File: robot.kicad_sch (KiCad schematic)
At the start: 31 parts, among them M1 MOTOR, M2 MOTOR, M3 MOTOR, M4 MOTOR, M5 MOTOR, M6 SERVO, U1 BUCKCONVERTER, U12 MEEN3230_POWER_BOARD, U2 TCS3200, U3 XBEE_DONGLE, U6 SHARPDISTANCE, U7 HALL-EFFECT

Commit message: greatly cleaned up electrical schematic
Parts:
- removed D1, D2, D3: SINGLETB9051FTG_MOTOR_DRIVER, SINGLETB9051FTG_MOTOR_DRIVER:SINGLETB9051FTG, symbol ME3230:SINGLETB9051FTG_MOTOR_DRIVER
- removed M1, M2, M3: MOTOR, MOTOR:VIBE-MOTOR-10MM, symbol ME3230:MOTOR
- removed ME1, ME2, ME3: ENCODER, ENCODER:ENCODER, symbol ME3230:ENCODER
- added J1, J4, J6: Conn_02x06_Top_Bottom, symbol Connector_Generic:Conn_02x06_Top_Bottom
- added J2: Conn_02x18_Counter_Clockwise, symbol Connector_Generic:Conn_02x18_Counter_Clockwise
- added M7, M8, M9: MOTOR, MOTOR:VIBE-MOTOR-10MM, symbol ME3230:MOTOR
- added U10, U4, U8: SINGLETB9051FTG_MOTOR_DRIVER, SINGLETB9051FTG_MOTOR_DRIVER:SINGLETB9051FTG, symbol ME3230:SINGLETB9051FTG_MOTOR_DRIVER
- added U11, U5, U9: ENCODER, ENCODER:ENCODER, symbol ME3230:ENCODER
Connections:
- net +5V: now also J1.4 (Pin_4), J4.4 (Pin_4), J6.4 (Pin_4), U10.P4 (VCC), U4.P4 (VCC), U8.P4 (VCC)
- net +9V: now also U10.P11 (VIN), U4.P11 (VIN), U8.P11 (VIN)
- net A3: now also J2.4 (Pin_4)
- net A4: now also J2.10 (Pin_10)
- net A5: now also J2.16 (Pin_16)
- net D18: now also J2.12 (Pin_12)
- net D19: now also J2.11 (Pin_11)
- net D2: now also J2.6 (Pin_6)
- net D20: now also J2.18 (Pin_18)
- net D21: now also J2.17 (Pin_17)
- net D3: now also J2.5 (Pin_5)
- net D38: now also J2.2 (Pin_2)
- net D39: now also J2.3 (Pin_3)
- net D40: now also J2.8 (Pin_8)
- net D41: now also J2.9 (Pin_9)
- net D42: now also J2.14 (Pin_14)
- net D43: now also J2.15 (Pin_15)
- net D6: now also J2.1 (Pin_1)
- net D7: now also J2.7 (Pin_7)
- net D8: now also J2.13 (Pin_13)
- net GND: now also J1.3 (Pin_3), J4.3 (Pin_3), J6.3 (Pin_3), U10.P12 (MGND), U10.P5 (GND), U4.P12 (MGND), U4.P5 (GND), U8.P12 (MGND), U8.P5 (GND)
- new net: J4.1 (Pin_1), U8.P13 (OUT2)
- new net: J4.10 (Pin_10), U9.P4 (VIN)
- new net: J4.11 (Pin_11), U9.P3 (OUTB)
- new net: J4.12 (Pin_12), U9.P2 (OUTA)
- new net: J4.2 (Pin_2), U8.P14 (OUT1)
- new net: J4.7 (Pin_7), M8.+
- new net: J4.8 (Pin_8), M8.-
- new net: J4.9 (Pin_9), U9.P1 (GND)
- new net: J1.9 (Pin_9), U5.P1 (GND)
- new net: J1.12 (Pin_12), U5.P2 (OUTA)
- new net: J1.11 (Pin_11), U5.P3 (OUTB)
- new net: J1.10 (Pin_10), U5.P4 (VIN)
- new net: J1.1 (Pin_1), U4.P13 (OUT2)
- new net: J1.2 (Pin_2), U4.P14 (OUT1)
- new net: J1.7 (Pin_7), M7.+
- new net: J1.8 (Pin_8), M7.-
- new net: J6.9 (Pin_9), U11.P1 (GND)
- new net: J6.12 (Pin_12), U11.P2 (OUTA)
- new net: J6.11 (Pin_11), U11.P3 (OUTB)
- new net: J6.10 (Pin_10), U11.P4 (VIN)
- new net: J6.1 (Pin_1), U10.P13 (OUT2)
- new net: J6.2 (Pin_2), U10.P14 (OUT1)
- new net: J6.7 (Pin_7), M9.+
- new net: J6.8 (Pin_8), M9.-
- new net M1_1: J2.36 (Pin_36), U4.P2 (EN)
- new net M1_2: J2.35 (Pin_35), U4.P7 (PWM2)
- new net M1_3: J2.34 (Pin_34), U4.P8 (PWM1)
- new net M1_4: J2.33 (Pin_33), U4.P9 (OCM)
- new net M1_5: J1.5 (Pin_5), J2.32 (Pin_32)
- new net M1_6: J1.6 (Pin_6), J2.31 (Pin_31)
- new net M2_1: J2.30 (Pin_30), U8.P2 (EN)
- new net M2_2: J2.29 (Pin_29), U8.P7 (PWM2)
- new net M2_3: J2.28 (Pin_28), U8.P8 (PWM1)
- new net M2_4: J2.27 (Pin_27), U8.P9 (OCM)
- new net M2_5: J2.26 (Pin_26), J4.5 (Pin_5)
- new net M2_6: J2.25 (Pin_25), J4.6 (Pin_6)
- new net M3_1: J2.24 (Pin_24), U10.P2 (EN)
- new net M3_2: J2.23 (Pin_23), U10.P7 (PWM2)
- new net M3_3: J2.22 (Pin_22), U10.P8 (PWM1)
- new net M3_4: J2.21 (Pin_21), U10.P9 (OCM)
- new net M3_5: J2.20 (Pin_20), J6.5 (Pin_5)
- new net M3_6: J2.19 (Pin_19), J6.6 (Pin_6)
- no-connect marks 45 -> 54
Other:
- note added: "18-Wide Ribbon Cable to Arduino"
- note added: "1: PWM 2: Control 1 3: Control 2 4: Current Reading 5: Encoder B 6: Encoder A"
- note added: "Button Presser Front of Robot"
- note added: "Everything In Here Is Rigidly Attached to the Base"
- note added: "For Motors Red: Power+, Black: Power- Green: GND, Blue: Encoder VCC (5V) Yellow/White: Encoder Outputs"
- note added: "IR Reflectance Array Bottom of Robot"
- note added: "In Shovel"
- note added: "Logic Power from Buck"
- note added: "Motors Ground"
- note added: "Power from Battery"
- note added: "Range-Finder Back of Robot"
- note added: "This Shit Movin'"
- moved on the sheet: B1, BT1, D4, Di1, Di2, F1, M4, M5, M6, R1, R2, R3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

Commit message: Forgot to update kicad schematic to match pin changes
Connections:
- net A1: no longer R2.P4 (O1)
- net A2: no longer R3.P4 (O1)
- net D34: now also R3.P4 (O1); no longer R2.P3 (CTRL)
- net D36: now also R2.P4 (O1); no longer R3.P3 (CTRL)
- no-connect marks 54 -> 58
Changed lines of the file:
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@@
 	)
 	(no_connect
+		(at 340.36 78.74)
+	)
+	(no_connect
 		(at 33.02 133.35)
 	)
@@
 	)
 	(no_connect
+		(at 341.63 120.65)
+	)
+	(no_connect
 		(at 33.02 128.27)
 	)
@@
 	)
 	(no_connect
+		(at 33.02 115.57)
+	)
+	(no_connect
 		(at 170.18 102.87)
 	)
@@
 	)
 	(no_connect
+		(at 33.02 113.03)
+	)
+	(no_connect
 		(at 106.68 57.15)
 	)
@@
 	(wire
 		(pts
-			(xy 332.74 78.74) (xy 340.36 78.74)
-		)
-		(stroke
-			(width 0)
-			(type default)
-		)
-	)
-	(wire
-		(pts
 			(xy 69.85 135.89) (xy 80.01 135.89)
 		)
@@
 		)
 	)
-	(wire
-		(pts
-			(xy 334.01 120.65) (xy 341.63 120.65)
-		)
-		(stroke
-			(width 0)
-			(type default)
-		)
-	)
 	(label "D45"
 		(at 327.66 41.91 0)
@@
 		)
 	)
-	(label "A2"
-		(at 334.01 123.19 0)
-		(effects
-			(font
-				(size 1.27 1.27)
-			)
-			(justify left bottom)
-		)
-	)
 	(label "D34"
-		(at 332.74 78.74 0)
+		(at 334.01 123.19 0)
 		(effects
 			(font
@@
 		)
 	)
-	(label "A1"
+	(label "D36"
 		(at 332.74 81.28 0)
 		(effects
@@
 		)
 	)
-	(label "D36"
-		(at 334.01 120.65 0)
-		(effects
-			(font
-				(size 1.27 1.27)
-			)
-			(justify left bottom)
-		)
-	)

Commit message: Added discard servo to schematic
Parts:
- added M1: SERVO, SERVO:SERVOFOOTPRINT, symbol ME3230:SERVO
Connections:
- net +5V: now also M1. (V+)
- net D12: now also M1. (V+)
- net GND: now also M1. (V+)
- no-connect marks 58 -> 57
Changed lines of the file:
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@@
 	)
 	(no_connect
-		(at 80.01 107.95)
-	)
-	(no_connect
 		(at 170.18 158.75)
 	)
@@
 	(wire
 		(pts
+			(xy 259.08 140.97) (xy 269.24 140.97)
+		)
+		(stroke
+			(width 0)
+			(type default)
+		)
+	)
+	(wire
+		(pts
 			(xy 222.25 203.2) (xy 226.06 203.2)
 		)
@@
 		)
 	)
+	(label "D12"
+		(at 259.08 140.97 0)
+		(effects
+			(font
+				(size 1.27 1.27)
+			)
+			(justify left bottom)
+		)
+	)
 	(label "D50"
 		(at 370.84 27.94 270)
@@
 	)
 	(symbol
+		(lib_name "SERVO_1")
+		(lib_id "ME3230:SERVO")
+		(at 271.78 140.97 180)
+		(unit 1)
+		(exclude_from_sim no)
+		(in_bom yes)
+		(on_board yes)
+		(dnp no)
+		(fields_autoplaced yes)
+		(property "Reference" "M1"
+			(at 290.83 137.1599 0)
+			(effects
+				(font
+					(size 1.27 1.27)
+				)
+				(justify right)
+			)
+		)
+		(property "Value" "SERVO"
+			(at 290.83 139.6999 0)
+			(effects
+				(font
+					(size 1.27 1.27)
+				)
+				(justify right)
+			)
+		)
+		(property "Footprint" "SERVO:SERVOFOOTPRINT"
+			(at 273.304 146.558 0)
+			(effects
+				(font
+					(size 1.27 1.27)
+				)
+				(justify bottom)
+				(hide yes)
+			)
+		)
+		(property "Datasheet" ""
+			(at 271.78 140.97 0)
+			(effects
+				(font
+					(size 1.27 1.27)
+				)
+				(hide yes)
+			)
+		)
+		(property "Description" ""
+			(at 271.78 140.97 0)
+			(effects
+				(font
+					(size 1.27 1.27)
+				)
+				(hide yes)
+			)
+		)
+		(pin ""
+		)
+		(pin ""
+		)
+		(pin ""
+		)
+		(instances
+			(project ""
+				(path "/c33baf39-1524-47fd-8733-9db21030ba51"
+					(reference "M1")
+					(unit 1)
+				)
+			)
+		)
+	)
+	(symbol
 		(lib_id "power:GND")
 		(at 340.36 73.66 270)
@@
 	)
 	(symbol
+		(lib_id "power:+5V")
+		(at 269.24 138.43 90)
+		(unit 1)
+		(exclude_from_sim no)
+		(in_bom yes)
+		(on_board yes)
+		(dnp no)
+		(fields_autoplaced yes)
+		(property "Reference" "#PWR07"
+			(at 273.05 138.43 0)
+			(effects
+				(font
+					(size 1.27 1.27)
+				)
+				(hide yes)
+			)
+		)
+		(property "Value" "+5V"
+			(at 265.43 138.4299 90)
+			(effects
+				(font
+					(size 1.27 1.27)
+				)
+				(justify left)
+			)
+		)
+		(property "Footprint" ""
+			(at 269.24 138.43 0)
+			(effects
+				(font
+					(size 1.27 1.27)
+				)
+				(hide yes)
+			)
+		)
+		(property "Datasheet" ""
+			(at 269.24 138.43 0)
+			(effects
+				(font
+					(size 1.27 1.27)
+				)
+				(hide yes)
+			)
+		)
+		(property "Description" "Power symbol creates a global label with name \"+5V\""
+			(at 269.24 138.43 0)
+			(effects
+				(font
+					(size 1.27 1.27)
+				)
+				(hide yes)
+			)
+		)
+		(pin "1"
+		)
+		(instances
+			(project ""
+				(path "/c33baf39-1524-47fd-8733-9db21030ba51"
+					(reference "#PWR07")
+					(unit 1)
+				)
+			)
+		)
+	)
+	(symbol
 		(lib_id "ME3230:ENCODER")
 		(at 232.41 166.37 0)
@@
 					(unit 1)
 				)
+			)
+		)
+	)
+	(symbol
+		(lib_id "power:GND")
+		(at 269.24 135.89 270)
+		(unit 1)
+		(exclude_from_sim no)
+		(in_bom yes)
+		(on_board yes)
+		(dnp no)
+		(fields_autoplaced yes)
+		(property "Reference" "#PWR06"
+			(at 262.89 135.89 0)
+			(effects
+				(font
+					(size 1.27 1.27)
+				)
+				(hide yes)
+			)
+		)
+		(property "Value" "GND"
+			(at 265.43 135.8899 90)
+			(effects
+				(font
+					(size 1.27 1.27)
+				)
+				(justify right)
+			)
+		)
+		(property "Footprint" ""
+			(at 269.24 135.89 0)
+			(effects
+				(font
+					(size 1.27 1.27)
+				)
+				(hide yes)
+			)
+		)
+		(property "Datasheet" ""
+			(at 269.24 135.89 0)
+			(effects
+				(font
+					(size 1.27 1.27)
+				)
+				(hide yes)
+			)
+		)
+		(property "Description" "Power symbol creates a global label with name \"GND\" , ground"
+			(at 269.24 135.89 0)
+			(effects
+				(font
+					(size 1.27 1.27)
+				)
+				(hide yes)
+			)
+		)
+		(pin "1"
+		)
+		(instances
+			(project ""
+				(path "/c33baf39-1524-47fd-8733-9db21030ba51"
+					(reference "#PWR06")
+					(unit 1)
+				)

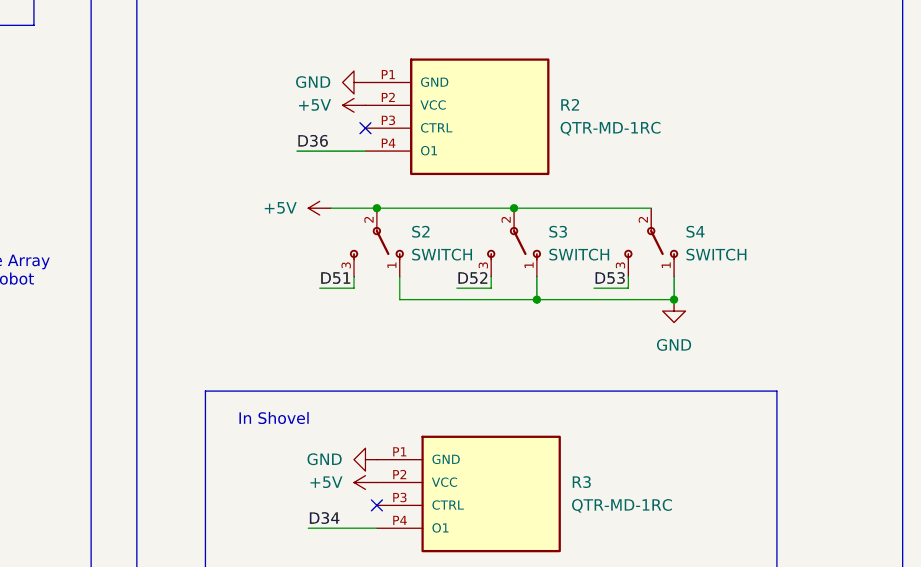
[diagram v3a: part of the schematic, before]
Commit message: Switched to pull-up limit-switches
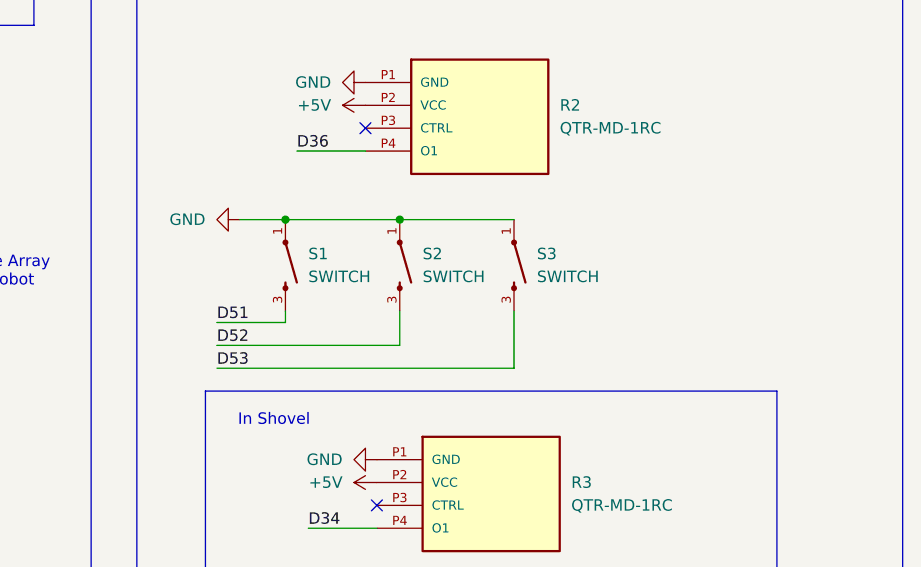
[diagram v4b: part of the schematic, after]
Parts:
- removed S2, S3, S4: SWITCH, SWITCH-SPDT:SWITCH_SPDT_SMD, symbol ME3230:SWITCH-SPDT
- added S1, S2, S3: SWITCH, MechLibrary:Header3, symbol ME3230:PUSHBUTTON-SWITCH
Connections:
- net D51: now also S1.3
- net D52: now also S2.3
- net D53: now also S3.3
- net GND: now also S1.1, S2.1, S3.1

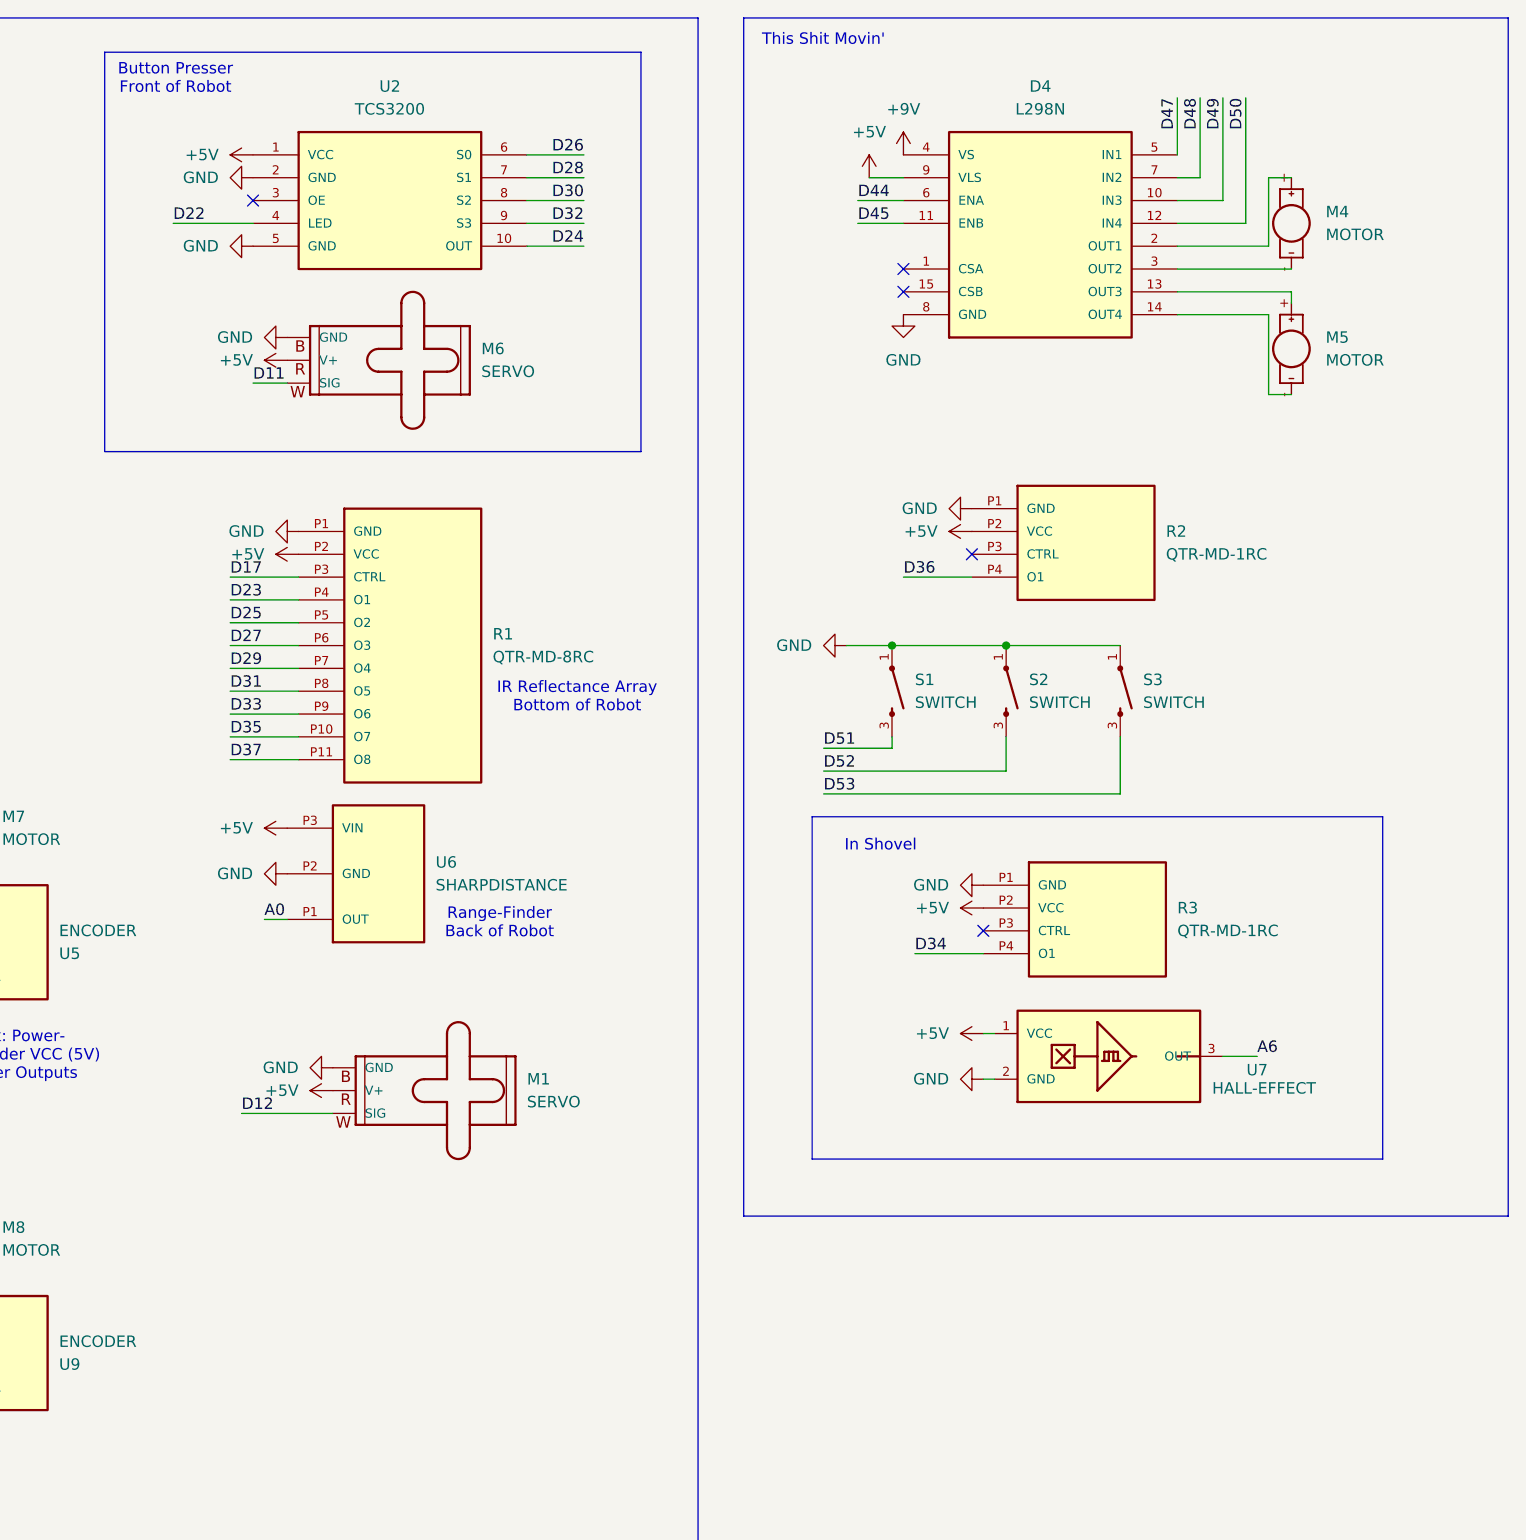
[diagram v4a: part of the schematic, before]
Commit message: removed tertiary limit switch
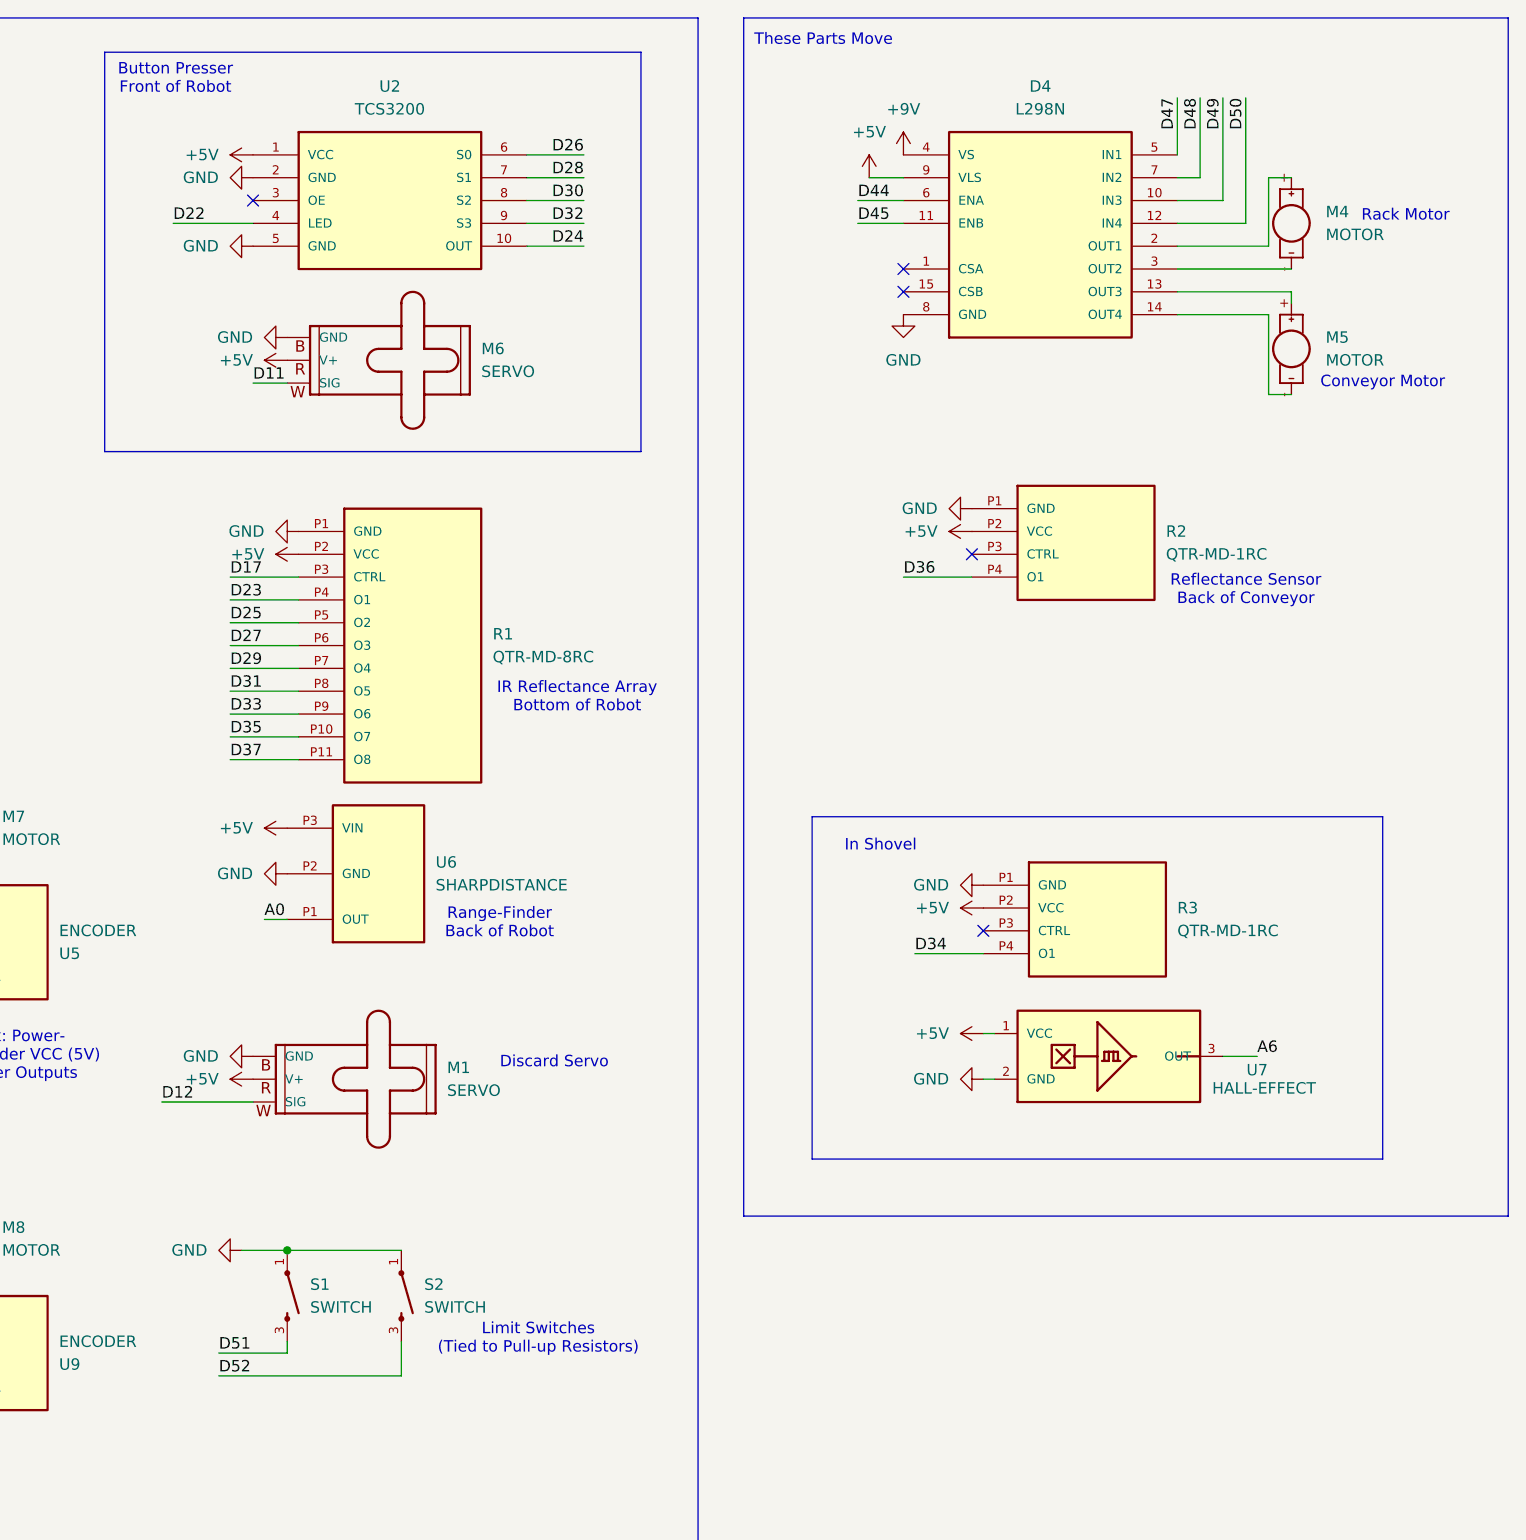
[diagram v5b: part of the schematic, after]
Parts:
- removed S3: SWITCH, MechLibrary:Header3, symbol ME3230:PUSHBUTTON-SWITCH
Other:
- note added: "Conveyor Motor"
- note added: "Discard Servo"
- note added: "Limit Switches (Tied to Pull-up Resistors)"
- note added: "Rack Motor"
- note added: "Reflectance Sensor Back of Conveyor"
- note added: "These Parts Move"
- note removed: "This Shit Movin'"
- moved on the sheet: M1, S1, S2
